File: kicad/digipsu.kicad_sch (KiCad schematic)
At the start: 61 parts, among them J1 Screw_Terminal_01x03, J2 PWR IN, Q1 BC337, Q2 BC327, Q3 2N6058, Q4 2N6058, Q5 IRLZ34N, U1 INA169, U2 MCP6002-xP, U3 Pico, U4 MCP6002-xP

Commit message: Update design
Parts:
- removed NT7: NetTie_2, Personal:NetTie_5mm_0.635mm, symbol Device:NetTie_2
- removed R30, R31: 2K2, Resistor_THT:R_Axial_DIN0207_L6.3mm_D2.5mm_P2.54mm_Vertical, symbol Device:R
- added C4, C5: C, symbol Device:C
- added NT1: NetTie_2, Personal:NetTie_5mm_0.635mm, symbol Device:NetTie_2
- added R39: 10k, Resistor_THT:R_Axial_DIN0207_L6.3mm_D2.5mm_P7.62mm_Horizontal, symbol Device:R
- added R40: 1k, Resistor_THT:R_Axial_DIN0207_L6.3mm_D2.5mm_P7.62mm_Horizontal, symbol Device:R
- added R41: 200, Potentiometer_THT:Potentiometer_Bourns_3296W_Vertical, symbol Device:R_Potentiometer_Trim
- added U5: L7805, symbol Regulator_Linear:L7805
- added U6: 4066, symbol 4xxx:4066
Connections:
- net +5V: now also C5.1, U5.3 (OUT)
- net CurrentSenseX10: now also R39.1
- net DAC1: now also R32.2; no longer R10.2, R11.2
- net DAC2: now also R11.2; no longer R13.2, R14.2
- net DAC3: now also R12.2; no longer R16.2, R17.2
- net DAC4: now also R13.2; no longer R19.2, R20.2
- net DAC5: now also R26.2; no longer R22.2, R23.2
- net DAC6: now also R27.2; no longer R25.2, R26.2
- net DAC7: no longer R29.2
- net DAC8: now also R29.2; no longer R32.2
- net GND: now also R33.2, C5.2, NT1.2, R40.2; no longer C1.2, R9.2
- net at U4.5 (+): now also C2.1, L1.2, R4.1, R8.1
- net at NT3.1, NT4.1, R1.2: now also J1.1 (Pin_1); no longer J1.3 (Pin_3)
- net at R14.1, R15.1: now also R12.1, R16.2, R17.2; no longer R12.2, R13.1
- net at R16.1, R17.1: now also R13.1, R18.2, R19.2; no longer R15.2, R18.1
- net at R22.1, R23.1: now also R24.2, R25.2, R28.1; no longer R21.2, R24.1
- net GNDPWR: now reaches C2.2, C3.2, D1.2 (A), J2.1 (Pin_1), NT5.1
- net GNDPWR: now also C1.2, J1.3 (Pin_3), C4.2, NT1.1, U5.2 (GND); no longer J1.1 (Pin_1)
- net at R20.1, R21.1: now also R22.2, R23.2, R27.1; no longer R18.2, R19.1
- net VBUS: now reaches C3.1, F1.1, Q5.2 (D)
- net VBUS: now also NT6.2, C4.1, U5.1 (IN); no longer NT6.1
- net at R32.1, R33.1: now also R10.2, R9.2
- net at U2.6 (-): now also R39.2, R41.2
- net at Q2.3 (E), R7.1: now also NT6.1; no longer NT6.2
- net at R10.1, R11.1, R9.1: now also R14.2, R15.2; no longer R12.1
- net Control voltage: no longer names the net of Q1.2 (B)
- net Control voltage: now also R24.1, R25.1, R29.1; no longer R33.2
- new net: R40.1, R41.1
- new net: R18.1, R19.1, R20.2, R21.2, R26.1
- no-connect marks 2 -> 3
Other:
- note added: "Control voltage amplifier (0-3.3V to 0-33V)"
- note added: "Divide by 10, from 0-30V to 0-3V"
- note added: "Main power supply"
- note added: "R-2R Digital to analog converter"
- note added: "TODO: Sense voltage between regulators"
- moved on the sheet: C1, C2, C3, D1, F1, J1, J2, L1, Q1, Q2, Q3, Q4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

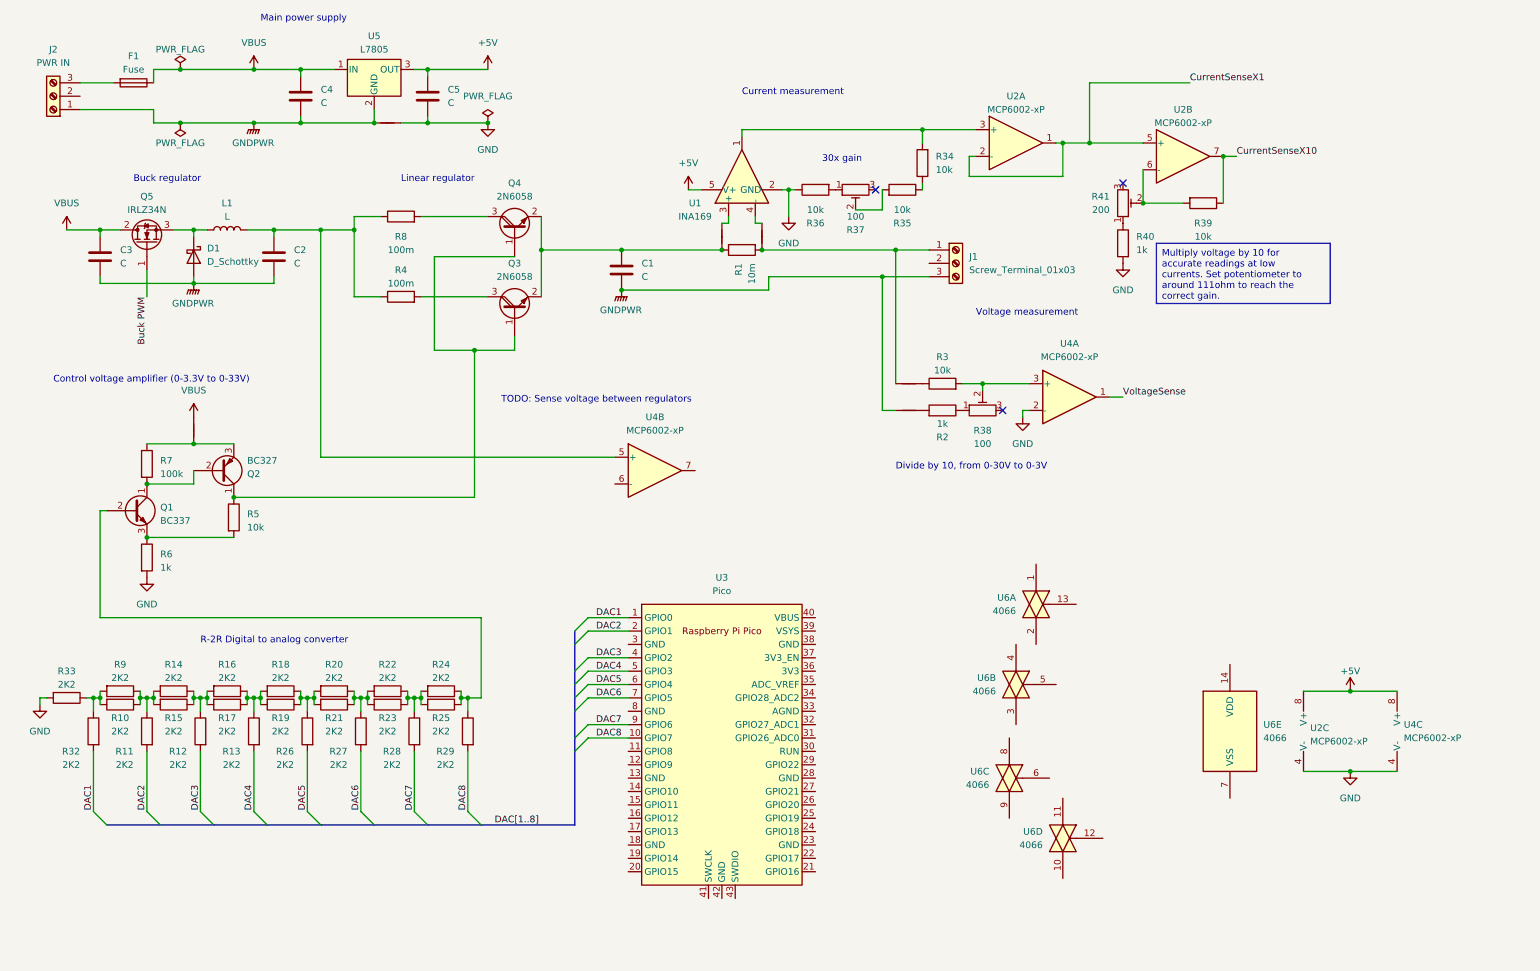
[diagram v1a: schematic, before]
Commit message: Complete controller board
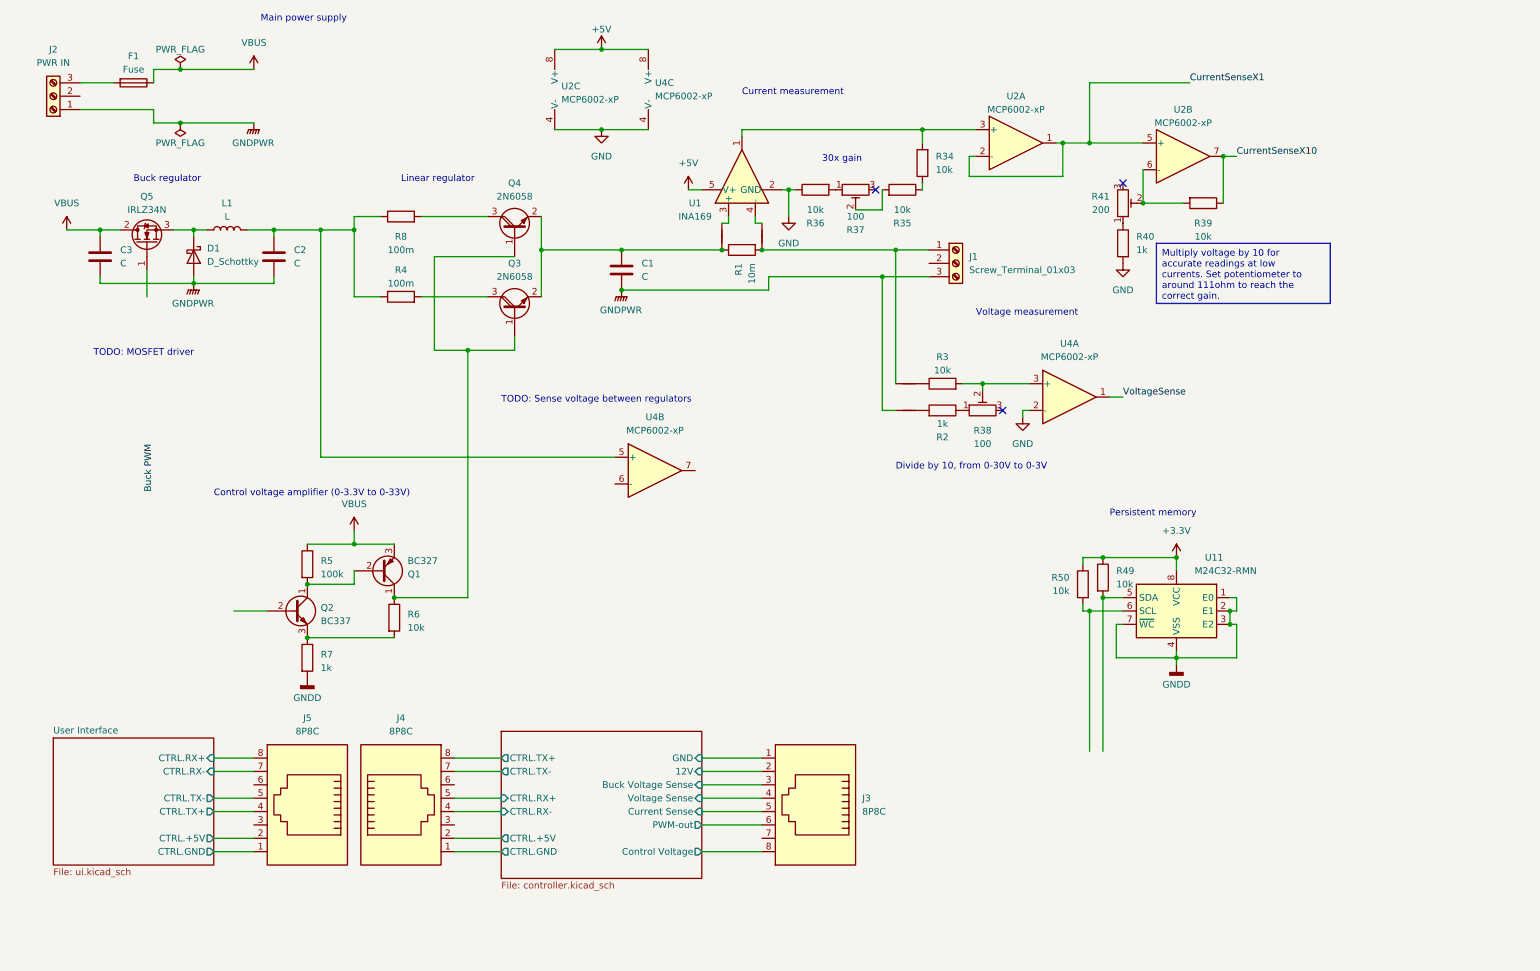
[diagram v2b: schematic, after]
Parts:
- removed C4, C5: C, symbol Device:C
- removed NT1, NT6: NetTie_2, Personal:NetTie_5mm_0.635mm, symbol Device:NetTie_2
- removed Q1: BC337, Package_TO_SOT_THT:TO-92_Inline, symbol Transistor_BJT:BC337
- removed Q2: BC327, Package_TO_SOT_THT:TO-92_Inline, symbol Transistor_BJT:BC327
- removed R10, R11, R12, R13, R14, R15, R16, R17, R18, R19, R20, R21, R22, R23, R24, R25, R26, R27, R28, R29, R32, R33, R9: 2K2, Resistor_THT:R_Axial_DIN0207_L6.3mm_D2.5mm_P2.54mm_Vertical, symbol Device:R
- removed U3: Pico, MCU_RaspberryPi_and_Boards:RPi_Pico_SMD_TH, symbol MCU_RaspberryPi_and_Boards:Pico
- removed U5: L7805, symbol Regulator_Linear:L7805
- removed U6: 4066, symbol 4xxx:4066
- added J3, J4, J5: 8P8C, Connector_RJ:RJ45_Amphenol_54602-x08_Horizontal, symbol Connector:8P8C
- added Q1: BC327, Package_TO_SOT_THT:TO-92_Inline, symbol Transistor_BJT:BC327
- added Q2: BC337, Package_TO_SOT_THT:TO-92_Inline, symbol Transistor_BJT:BC337
- added R49, R50: 10k, Resistor_THT:R_Axial_DIN0207_L6.3mm_D2.5mm_P7.62mm_Horizontal, symbol Device:R
- added U11: M24C32-RMN, Package_SO:SOIC-8_3.9x4.9mm_P1.27mm, symbol Memory_EEPROM:M24C02-RMN
- C1, C2, C3: footprint (none) -> Capacitor_THT:C_Disc_D3.8mm_W2.6mm_P2.50mm
- R5: value 10k -> 100k
- R6: value 1k -> 10k
- R7: value 100k -> 1k
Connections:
- net Buck PWM: no longer Q5.1 (G)
- net GND: no longer R6.2
- net VBUS: now also R5.1, Q1.3 (E)
- net GNDD: now reaches R7.2
- net GNDD: now also U11.1 (E0), U11.2 (E1), U11.3 (E2), U11.4 (VSS), U11.7 (~{WC})
- net at R5.2: now also Q1.2 (B), Q2.1 (C); no longer R6.1
- net at R7.1: now also R6.2, Q2.3 (E)
- net at Q3.1 (B), Q4.1 (B): now also R6.1, Q1.1 (C); no longer R5.1
- new net: R49.2, U11.5 (SDA)
- new net: R50.2, U11.6 (SCL)
- new net +3.3V: R49.1, R50.1, U11.8 (VCC)
- new net Controller/12V: J3.2
- new net Controller/Buck Voltage Sense: J3.3
- new net Controller/CTRL.+5V: J4.2
- new net Controller/CTRL.GND: J4.1
- new net Controller/CTRL.RX+: J4.5
- new net Controller/CTRL.RX-: J4.4
- new net Controller/CTRL.TX+: J4.8
- new net Controller/CTRL.TX-: J4.7
- new net Controller/Control Voltage: J3.8
- new net Controller/Current Sense: J3.5
- new net Controller/GND: J3.1
- new net Controller/PWM-out: J3.6
- new net Controller/Voltage Sense: J3.4
- new net User Interface/CTRL.+5V: J5.2
- new net User Interface/CTRL.GND: J5.1
- new net User Interface/CTRL.RX+: J5.8
- new net User Interface/CTRL.RX-: J5.7
- new net User Interface/CTRL.TX+: J5.4
- new net User Interface/CTRL.TX-: J5.5
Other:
- added sheet Controller (controller.kicad_sch)
- added sheet User Interface (ui.kicad_sch)
- note added: "Persistent memory"
- note added: "TODO: MOSFET driver"
- note removed: "R-2R Digital to analog converter"
- moved on the sheet: U2C, U4C

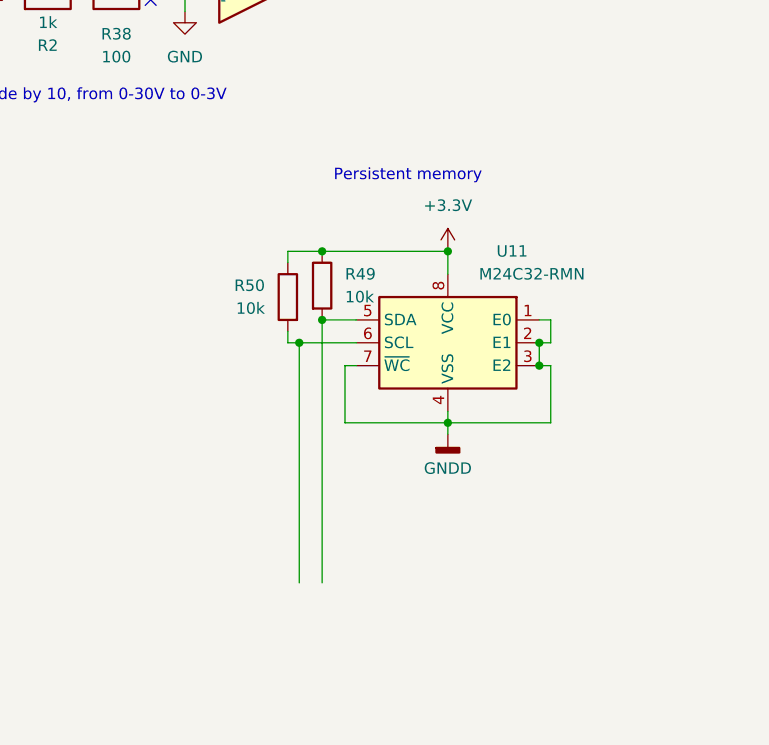
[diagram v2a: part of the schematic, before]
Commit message: Add kibot config
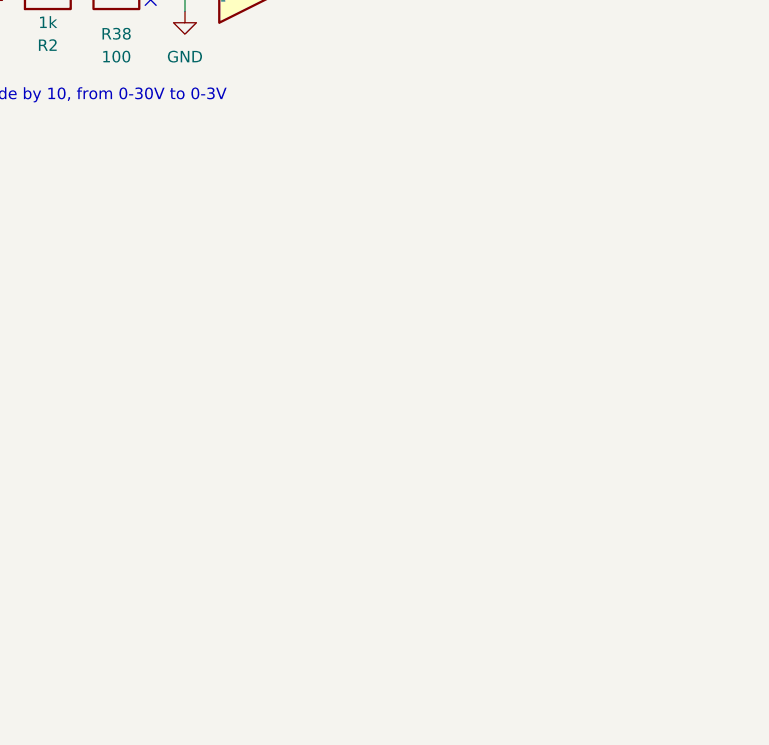
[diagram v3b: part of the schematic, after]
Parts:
- removed R49, R50: 10k, Resistor_THT:R_Axial_DIN0207_L6.3mm_D2.5mm_P7.62mm_Horizontal, symbol Device:R
- removed U11: M24C32-RMN, Package_SO:SOIC-8_3.9x4.9mm_P1.27mm, symbol Memory_EEPROM:M24C02-RMN
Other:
- note removed: "Persistent memory"

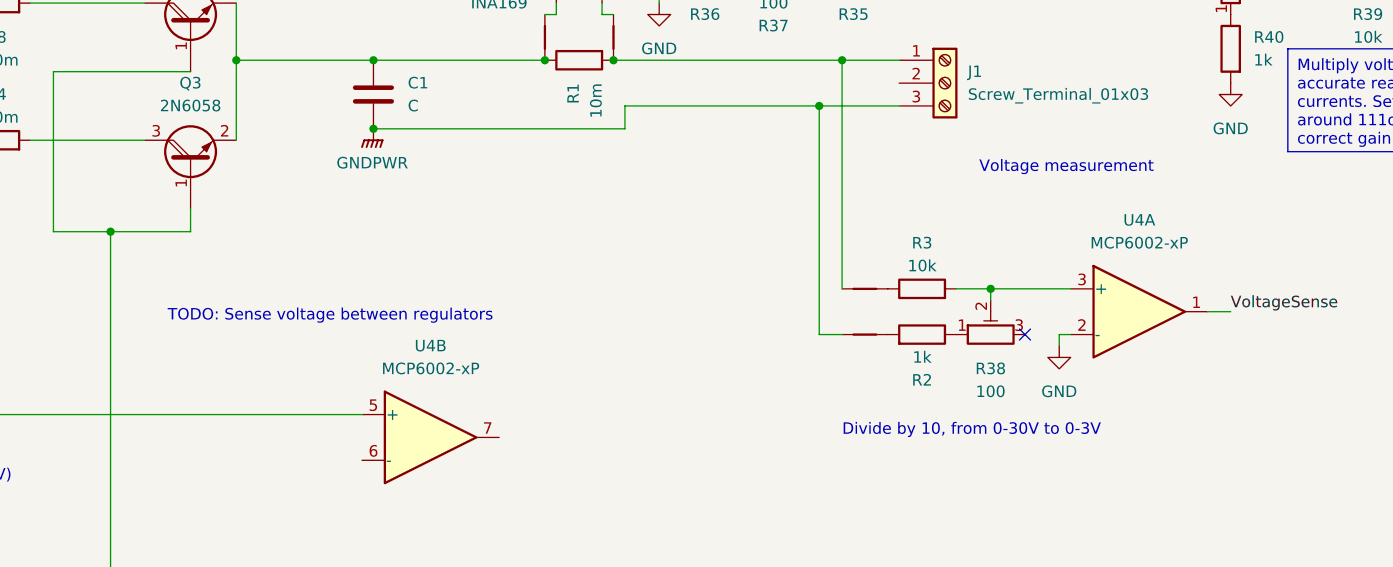
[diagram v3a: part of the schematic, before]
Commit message: Start UI pcb design
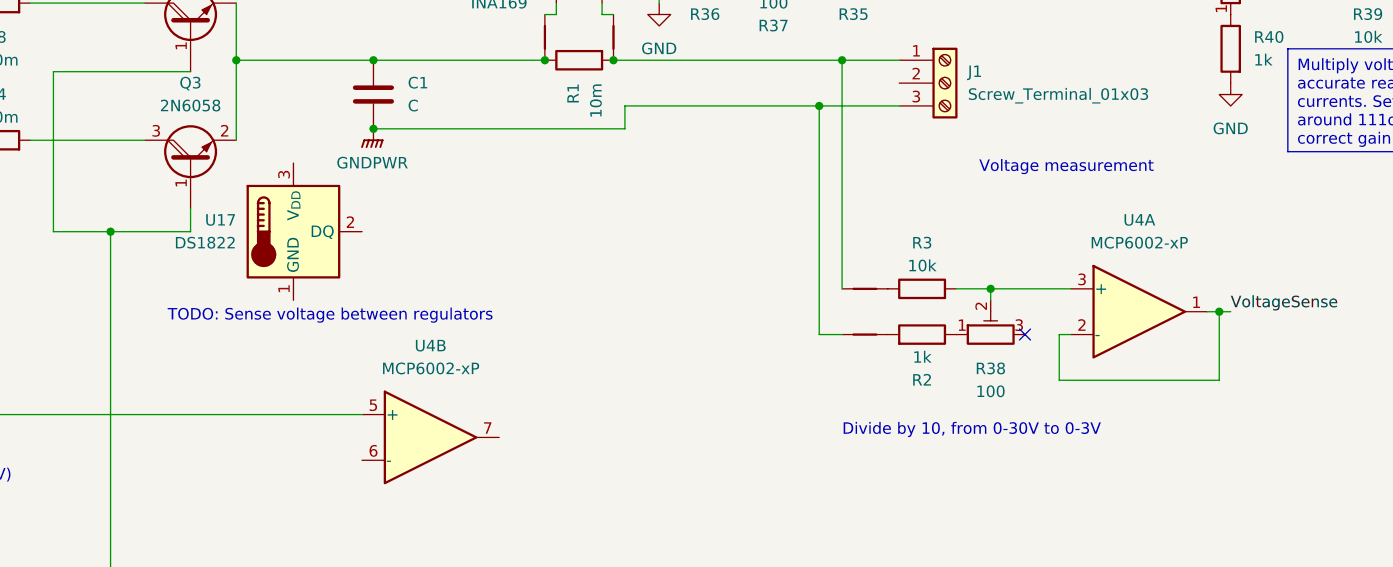
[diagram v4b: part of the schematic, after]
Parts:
- added U17: DS1822, Package_TO_SOT_THT:TO-92_Inline, symbol Sensor_Temperature:DS1822
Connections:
- net GND: no longer U4.2 (-)
- net VoltageSense: now also U4.2 (-)
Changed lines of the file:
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@@
   (junction (at 27.94 55.88) (diameter 0) (color 0 0 0 0)
+  )
+  (junction (at 220.98 87.63) (diameter 0) (color 0 0 0 0)
   )
   (junction (at 111.76 59.69) (diameter 0) (color 0 0 0 0)
@@
     (stroke (width 0) (type default))
   )
+  (wire (pts (xy 203.2 95.25) (xy 220.98 95.25))
+    (stroke (width 0) (type default))
+  )
   (wire (pts (xy 88.9 68.58) (xy 101.6 68.58))
     (stroke (width 0) (type default))
@@
     (stroke (width 0) (type default))
   )
+  (wire (pts (xy 220.98 87.63) (xy 222.25 87.63))
+    (stroke (width 0) (type default))
+  )
   (wire (pts (xy 95.25 163.83) (xy 104.14 163.83))
     (stroke (width 0) (type default))
@@
     (stroke (width 0) (type default))
   )
-  (wire (pts (xy 203.2 91.44) (xy 203.2 90.17))
+  (wire (pts (xy 203.2 90.17) (xy 203.2 95.25))
     (stroke (width 0) (type default))
   )
@@
     (stroke (width 0) (type default))
   )
+  (wire (pts (xy 220.98 95.25) (xy 220.98 87.63))
+    (stroke (width 0) (type default))
+  )
   (wire (pts (xy 179.07 59.69) (xy 179.07 85.09))
     (stroke (width 0) (type default))
@@
     (stroke (width 0) (type default))
   )
-  (wire (pts (xy 219.71 87.63) (xy 222.25 87.63))
+  (wire (pts (xy 219.71 87.63) (xy 220.98 87.63))
     (stroke (width 0) (type default))
   )
@@
     )
   )
+  (symbol (lib_id "Sensor_Temperature:DS1822") (at 118.11 78.74 0) (unit 1)
+    (in_bom yes) (on_board yes) (dnp no) (fields_autoplaced)
+    (property "Reference" "U17" (at 111.76 77.47 0)
+      (effects (font (size 1.27 1.27)) (justify right))
+    )
+    (property "Value" "DS1822" (at 111.76 80.01 0)
+      (effects (font (size 1.27 1.27)) (justify right))
+    )
+    (property "Footprint" "Package_TO_SOT_THT:TO-92_Inline" (at 92.71 85.09 0)
+      (effects (font (size 1.27 1.27)) hide)
+    )
+    (property "Datasheet" "http://datasheets.maximintegrated.com/en/ds/DS1822.pdf" (at 114.3 72.39 0)
+      (effects (font (size 1.27 1.27)) hide)
+    )
+    (pin "1")
+    (pin "2")
+    (pin "3")
+    (instances
+      (project "digipsu"
+        (path "/ec5fec7a-fde3-4f44-b689-61159deeeb72"
+          (reference "U17") (unit 1)
+        )
+      )
+    )
+  )
   (symbol (lib_id "Device:R") (at 184.15 43.18 180) (unit 1)
     (in_bom yes) (on_board yes) (dnp no) (fields_autoplaced)
@@
         )
       )
-    )
-  )
-  (symbol (lib_id "power:GND") (at 203.2 91.44 0) (unit 1)
-    (in_bom yes) (on_board yes) (dnp no) (fields_autoplaced)
-    (property "Reference" "#PWR07" (at 203.2 97.79 0)
-      (effects (font (size 1.27 1.27)) hide)
-    )
-    (property "Value" "GND" (at 203.2 96.52 0)
-      (effects (font (size 1.27 1.27)))
-    )
-    (property "Footprint" "" (at 203.2 91.44 0)
-      (effects (font (size 1.27 1.27)) hide)
-    )
-    (property "Datasheet" "" (at 203.2 91.44 0)
-      (effects (font (size 1.27 1.27)) hide)
-    )
-    (pin "1")
-    (instances
-      (project "digipsu"
-        (path "/ec5fec7a-fde3-4f44-b689-61159deeeb72"
-          (reference "#PWR07") (unit 1)
-        )
-      )

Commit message: Continue on UI board design
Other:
- note added: "TODO: Op-amp to drive power transistors"
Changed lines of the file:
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@@
+    (effects (font (size 1.27 1.27)) (justify left bottom))
+  )
+  (text "TODO: Op-amp to drive power transistors" (at 100.33 119.38 0)
     (effects (font (size 1.27 1.27)) (justify left bottom))
   )
